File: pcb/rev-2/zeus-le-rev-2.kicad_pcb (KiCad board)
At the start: 6 copper layers, 80 x 26 mm, 90 parts, among them J1 12402012E212A, J3 B2B-PH-SM4-TB, J4 B5B-PH-K-S, J5 BD125-10-A-0305-0580-L-B, J6 MSD-1-A, SW1 EVQPUD02K, U1 NUF2042XV6T1G, U10 LP5810ADSDR, U11 APS1604M-3SQR-ZR, U2 RT6160AWSC, U3 KTS1662EUW-TR, U4 BQ25150YFPR, U5 D3V3F4U6S-7, U6 TLV320ADC6120IRTER, U7 WT02C40C-V3, U8 AP21510FM-7, U9 TPD6F003DQDR

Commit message: pcb: full rev-2 layout
Mostly finished layout for the rev-2 board
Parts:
- moved JP4 0.12 mm to (146.4, 94.2)
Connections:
- net Net-(U7-P012) renamed /MCU/BUCKEN
- net Net-(U7-P031) renamed /MCU/IOVDD_CTRL
- JP4 pad 2: /MCU/RAM.~{CS} -> /MCU/SD.~{CS}
- U7 pad 11: /MCU/RAM.MOSI -> /MCU/SD.MOSI
- U7 pad A1: unconnected-(U7-P006-PadA1) -> /MCU/RAM.MOSI
- U7 pad A2: unconnected-(U7-P007-PadA2) -> /MCU/RAM.SCK
- U7 pad A3: /MCU/RAM.SCK -> /MCU/SD.SCK
- U7 pad A5: /MCU/SD.MISO -> /MCU/RAM.MISO
- U7 pad A6: /MCU/SD.MOSI -> /MCU/RAM.~{CS}
- U7 pad E6: /MCU/RAM.MISO -> /MCU/SD.MISO
- U7 pad Z5: /MCU/SD.SCK -> unconnected-(U7-P114-PadZ5)
- U7 pad Z6: /MCU/SD.~{CS} -> unconnected-(U7-P115-PadZ6)
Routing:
- net /MCU/RAM.~{CS}: track 7.57 -> 21.8 mm, vias 1 -> 2
- net /MCU/RAM.MOSI: track 4.43 -> 16.6 mm, vias 0 -> 2
- net /MCU/RAM.MISO: track 9.40 -> 21.5 mm
- net /MCU/SD.MOSI: track 15.2 -> 22.2 mm
- net /Power/VBAT: track 51.2 -> 56.8 mm, vias 7 -> 8
- net /MCU/SD.~{CS}: track 15.9 -> 20.9 mm, vias 2 -> 1
- net GND: track 56.6 -> 61.1 mm, vias 144 -> 158
- net /MCU/USB.D-: track 13.5 -> 15.5 mm
- net /MCU/RAM.SCK: track 16.0 -> 17.9 mm
- net /MCU/SD.SCK: track 17.3 -> 18.9 mm
- net /MCU/VDDD_VSEL: track 49.2 -> 47.7 mm
- net /MCU/SWCLK: track 37.5 -> 36.1 mm
- net /MCU/SD.MISO: track 15.7 -> 17.0 mm
- net /MCU/SD_EN: track 37.4 -> 38.6 mm
- net /MCU/CHG_EN: track 24.5 -> 23.4 mm
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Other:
- board text added: "P0.11/SWO"
- board text added: "VDDA_LDO"
- board text removed: "Debug"
- board text removed: "NC"
- board text removed: "RST"
- board text removed: "RX"
- board text removed: "SWCLK"
- board text removed: "SWDIO"
- board text removed: "SWO"
- board text removed: "TX"
- board text removed: "VDD"

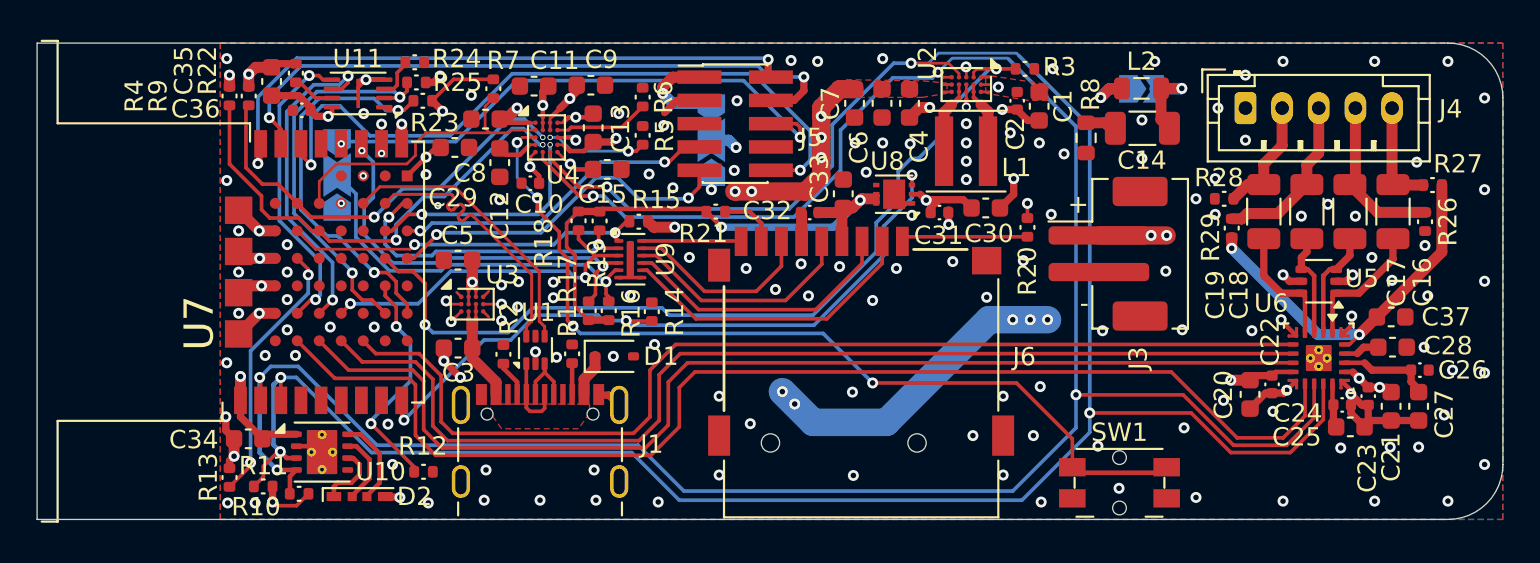
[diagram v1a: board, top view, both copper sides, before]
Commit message: pcb: update
Mostly downsize several decoupling capacitors to save space
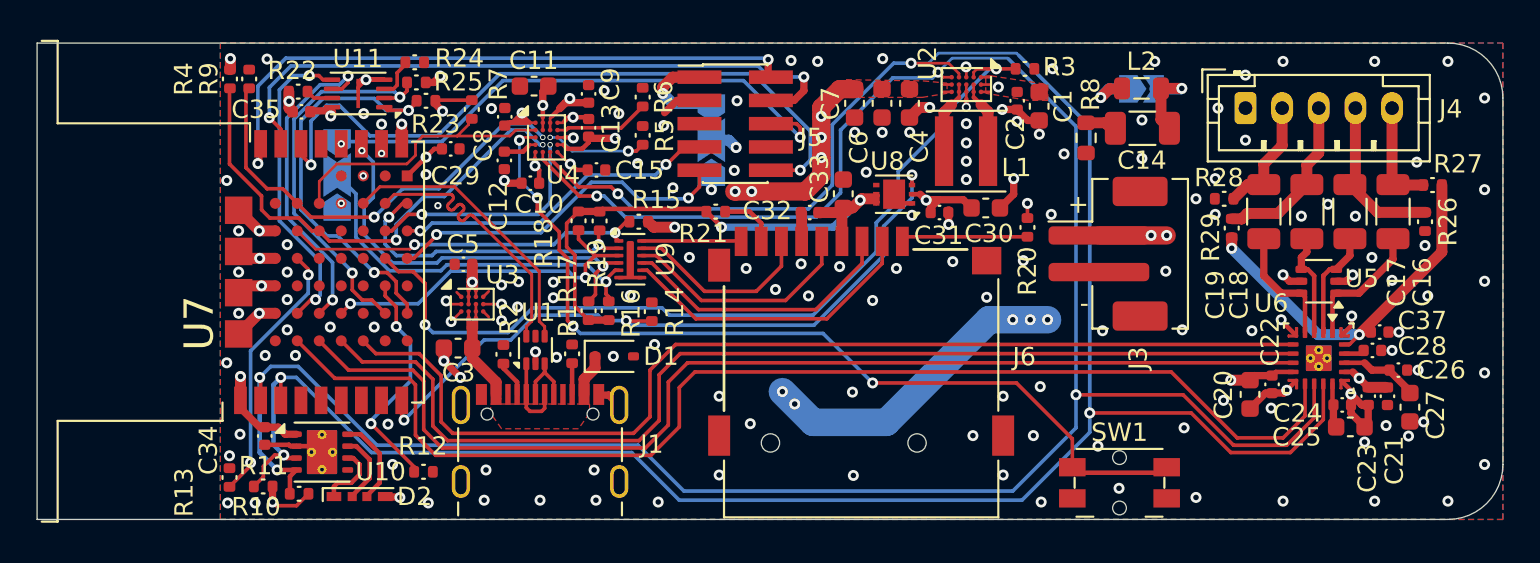
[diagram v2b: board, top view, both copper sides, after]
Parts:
- removed C36: 0.1µF, zeus-le:C_0402_1005Metric_Silkscreen_Clearance
- C11: value 10µF -> 22µF
- C12, C13, C15, C29, C8, C9: value 4.7µF -> 10µF; footprint Capacitor_SMD:C_0603_1608Metric -> zeus-le:C_0402_1005Metric_Silkscreen_Clearance
- C21, C28, C34, C35, C37, C5: value 1µF -> 2.2µF; footprint Capacitor_SMD:C_0603_1608Metric -> zeus-le:C_0402_1005Metric_Silkscreen_Clearance
- moved C35 2.32 mm to (144.4, 90.8), turned to 180 degrees
- moved R7 1.63 mm to (153.7, 90.6)
- moved C26 1.18 mm to (204.3, 104.8)
- moved C28 1.11 mm to (202.9, 103.8)
- moved C8 1.06 mm to (155.5, 91.0), turned to 90 degrees
- moved C37 1.04 mm to (203.3, 102.8)
- moved R22 1.02 mm to (144.2, 89.7), turned to 180 degrees
- moved R9 0.93 mm to (140.5, 89.0)
- moved R4 0.93 mm to (141.6, 89.0)
- moved C34 0.91 mm to (142.4, 108.4), turned to -90 degrees
- moved C15 0.59 mm to (160.5, 93.9)
- moved C21 0.59 mm to (203.7, 106.3)
- moved C9 0.49 mm to (160.1, 89.8), turned to 90 degrees
- moved C27 0.48 mm to (204.9, 106.9)
- moved C5 0.37 mm to (153.3, 99.1)
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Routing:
- net GND: track 61.1 -> 54.9 mm, vias 158 -> 160
- net VDDD: track 59.0 -> 53.0 mm
- net /Power/VBUS: track 18.0 -> 19.0 mm
- net /MCU/CHG_PG: track 16.7 -> 15.7 mm
- net /MCU/CHG_INT: track 25.9 -> 26.8 mm
- net Net-(U6-VREF): track 1.99 -> 1.12 mm
- net /Power/VBAT: track 56.8 -> 57.6 mm
- net Net-(U6-AREG): track 5.18 -> 4.39 mm
- net /MCU/CHG_EN: track 23.4 -> 24.1 mm
- net /Audio/I2C.SCL: track 131.4 -> 132.1 mm
- net /Audio/I2C.SDA: track 129.4 -> 130.1 mm
- net Net-(U11-SIO3): track 2.10 -> 1.48 mm
- net /MCU/RAM.~{CS}: track 21.8 -> 22.4 mm
- net VDDA: track 9.13 -> 8.88 mm, vias 4 -> 3

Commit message: Increase PSRAM size to 64Mbit
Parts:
- U11: value APS1604M-3SQR-ZR -> APS6404L-3SQR-ZR
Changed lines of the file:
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@@
 			)
 		)
-		(property "Value" "APS1604M-3SQR-ZR"
+		(property "Value" "APS6404L-3SQR-ZR"
 			(at 0 1.95 0)
 			(layer "F.Fab")
@@
 			)
 		)
-		(property "Datasheet" "https://www.apmemory.com/wp-content/uploads/APM_PSRAM_QSPI-APS1604M-3SQR-v2.7-PKG.pdf"
+		(property "Datasheet" "https://www.mouser.com/datasheet/2/1127/APM_PSRAM_QSPI_APS6404L_3SQR_v2_3_PKG-1954826.pdf"
 			(at 0 0 0)
 			(layer "F.Fab")
@@
 			)
 		)
-		(property "Description" "16 Mbit serial pseudo SRAM device organized as 2Mx8 bits, 3.3 VDD, USON-8"
+		(property "Description" "64 Mbit serial pseudo SRAM device organized as 8Mx8 bits, 3.3 VDD, USON-8"
 			(at 0 0 0)
 			(layer "F.Fab")

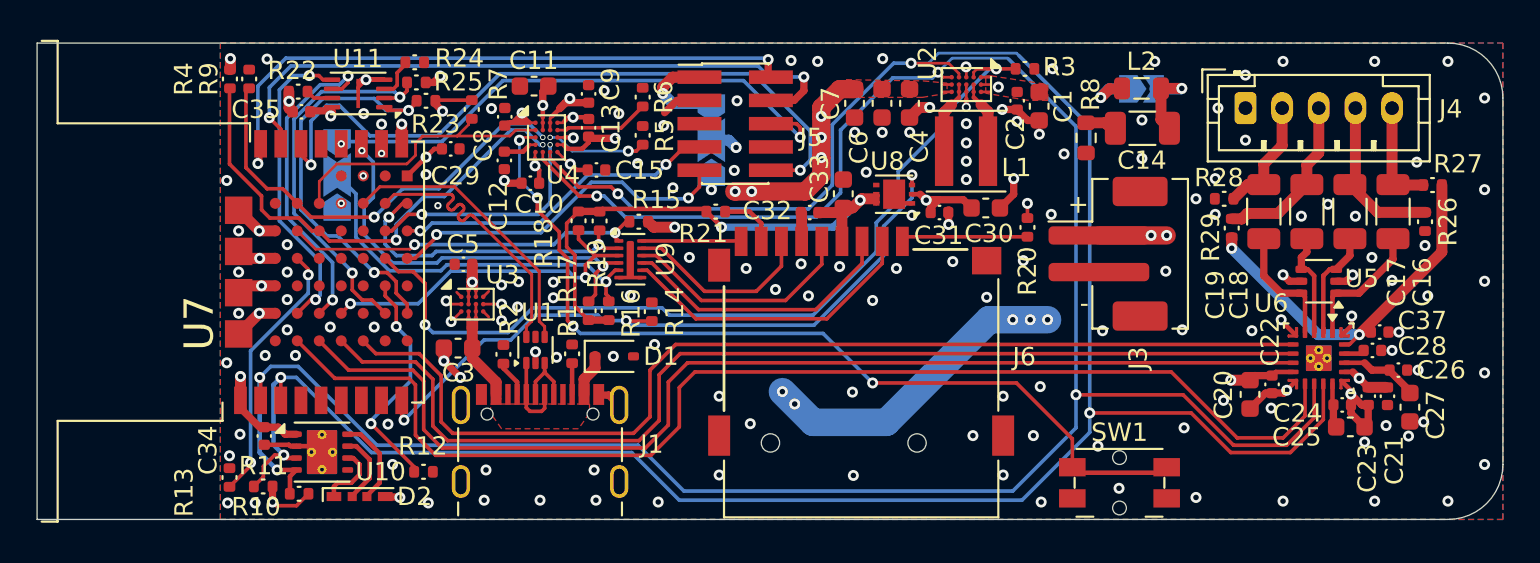
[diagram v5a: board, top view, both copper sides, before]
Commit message: Update PCBs
* Update to KiCad 10
* Update footprint for nRF53 module based on 1.01 datasheet with
  actually readable mechanical drawing
* Add 3D model for production nRF53 module
* Remove overlapping silkscreen on rev-1 with production nRF53 module
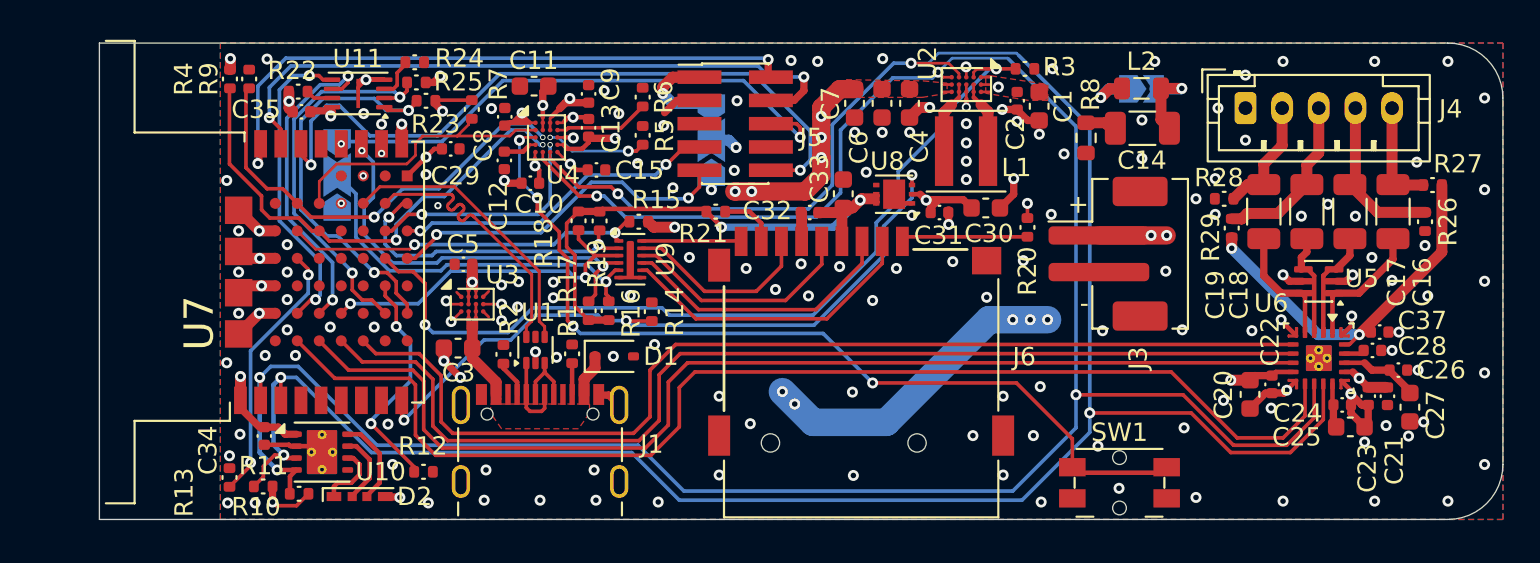
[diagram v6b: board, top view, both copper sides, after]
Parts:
- U7: value WT02C40C-V3 -> WT02C40C; footprint zeus-le:WT02C40C -> zeus-le:WT02C40C-VC
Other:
- board size 80 x 26 mm -> 76.6 x 26 mm
